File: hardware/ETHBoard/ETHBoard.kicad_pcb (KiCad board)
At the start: 2 copper layers, 25.1 x 12.2 mm, 24 parts, among them J1 Conn_02x04_Odd_Even, J2 Conn_01x02_Pin, U1 LAN8651B1-E_LMX, Y1 X322525MOB4SI

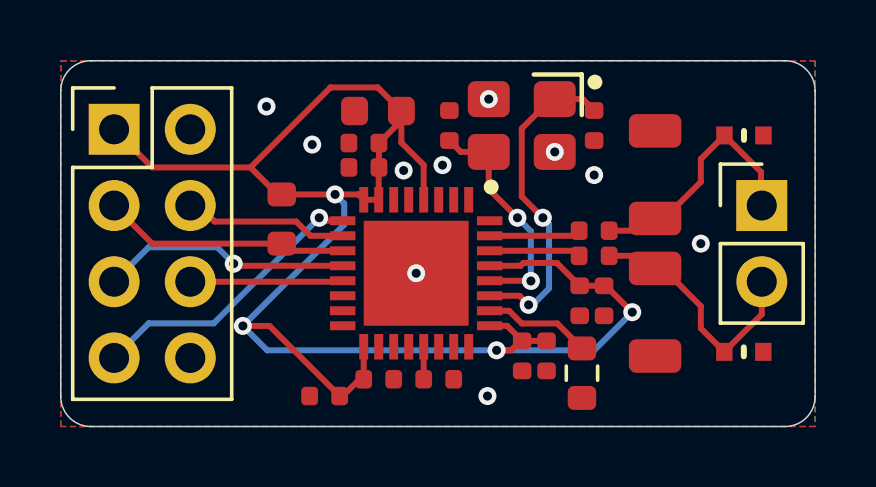
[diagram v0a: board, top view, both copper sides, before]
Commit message: Minor ETHBoard tweaks.
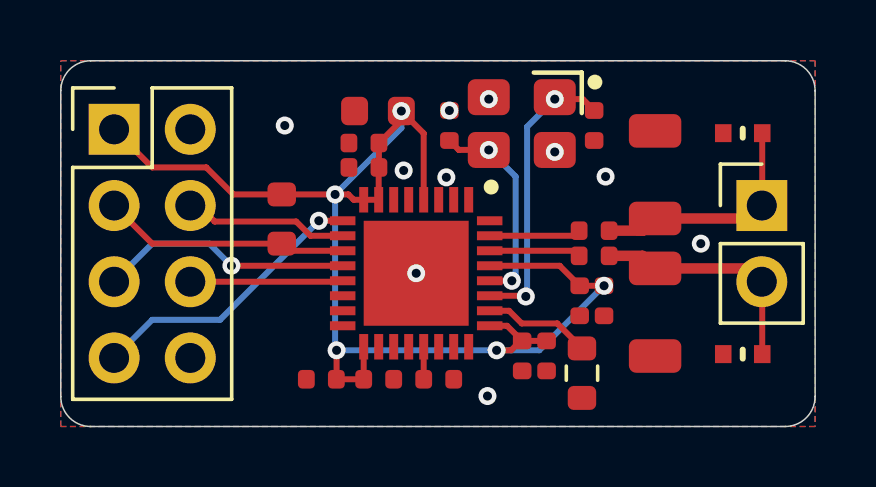
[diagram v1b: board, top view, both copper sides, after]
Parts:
- moved C11 0.57 mm to (82.3, 61.4)
- moved RV2 0.09 mm to (96.4, 53.2), turned to 180 degrees
- moved RV1 0.08 mm to (96.4, 60.6), turned to 180 degrees
- moved Y1 0.06 mm to (89.0, 52.9)
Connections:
- net Net-(J2-Pin_1) renamed /T1S_d-
- net Net-(J2-Pin_2) renamed /T1S_d+
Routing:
- net 3V3: track 57.4 -> 45.2 mm, vias 4 -> 5
- net Net-(U1-XTI): track 11.0 -> 9.67 mm
- net Net-(U1-XTO): track 7.73 -> 6.97 mm
- net /T1S_d-: track 8.46 -> 7.85 mm
- net /T1S_d+: track 8.45 -> 7.86 mm
